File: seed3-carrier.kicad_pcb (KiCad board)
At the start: 2 copper layers, 113 x 61.6 mm, 47 parts, among them J1 AudioJack2, J2 AudioJack2, J3 5V_IN, J4 DISPLAY_UART, J5 SJ1-3535NG, J6 Seed3_PINS_RIGHT, J7 Seed3_PINS_LEFT, U1 TLV9062IDR, U2 TPA6111A2DR

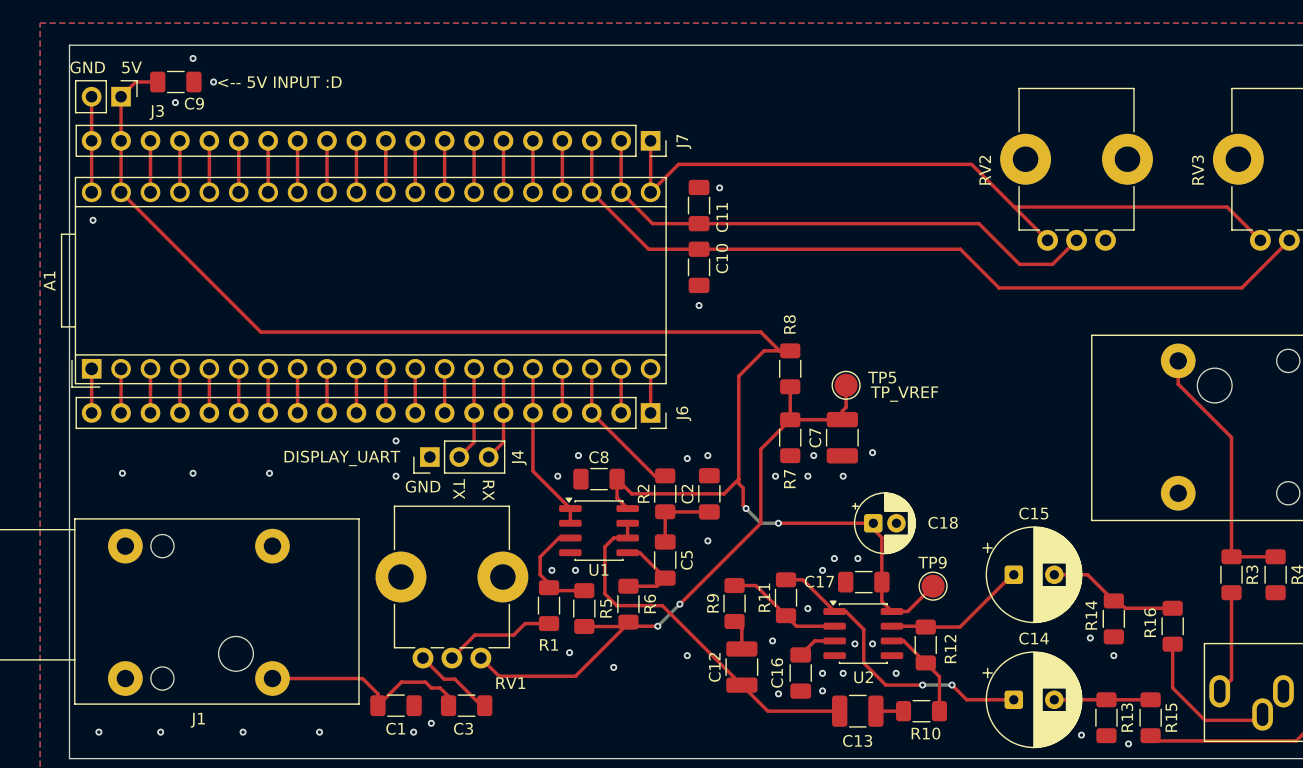
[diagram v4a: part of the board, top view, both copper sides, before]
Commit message: Reposition 5V connector and refine PCB routing
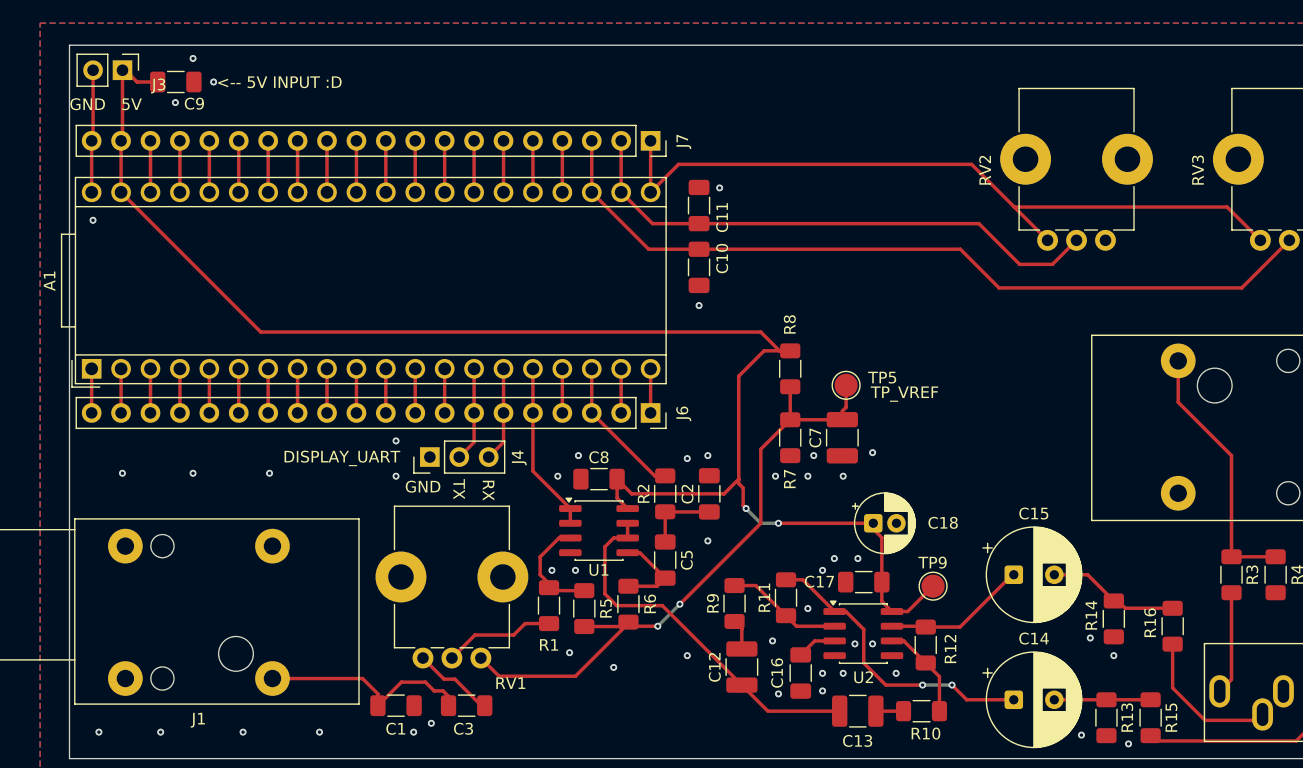
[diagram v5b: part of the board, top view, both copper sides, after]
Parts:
- moved J3 2.29 mm to (55.4, 42.2)
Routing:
- net GND: track 12.1 -> 14.4 mm
- net +5V: track 130.5 -> 132.6 mm
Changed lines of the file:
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@@
 	(footprint "Connector_PinHeader_2.54mm:PinHeader_1x02_P2.54mm_Vertical"
 		(layer "F.Cu")
-		(at 55.25 44.45 -90)
+		(at 55.377 42.164 -90)
 		(descr "Through hole straight pin header, 1x02, 2.54mm pitch, single row")
 		(tags "Through hole pin header THT 1x02 2.54mm single row")
@@
 	)
 	(gr_text "GND"
-		(at 50.8 42.545 0)
+		(at 50.8 45.72 0)
 		(layer "F.SilkS")
 		(effects
@@
 	)
 	(gr_text "5V"
-		(at 55.245 42.545 0)
+		(at 55.245 45.72 0)
 		(layer "F.SilkS")
 		(effects
@@
 	)
 	(segment
-		(start 100.975 67.945)
-		(end 100.975 71.755)
+		(start 52.837 48.138)
+		(end 52.715 48.26)
 		(width 0.3)
 		(layer "F.Cu")
@@
 	)
 	(segment
-		(start 52.715 52.705)
-		(end 52.715 48.26)
+		(start 52.837 42.164)
+		(end 52.837 48.138)
 		(width 0.3)
 		(layer "F.Cu")
@@
 	)
 	(segment
-		(start 52.71 48.255)
+		(start 100.975 67.945)
+		(end 100.975 71.755)
+		(width 0.3)
+		(layer "F.Cu")
+		(net "GND")
+	)
+	(segment
+		(start 52.715 52.705)
 		(end 52.715 48.26)
 		(width 0.3)
@@
 	)
 	(segment
-		(start 52.71 44.45)
-		(end 52.71 48.255)
+		(start 52.71 48.255)
+		(end 52.715 48.26)
 		(width 0.3)
 		(layer "F.Cu")
@@
 	)
 	(segment
-		(start 83.5275 96.2275)
-		(end 82.804 95.504)
+		(start 81.534 94.996)
+		(end 79.4635 94.996)
 		(width 0.3)
 		(layer "F.Cu")
@@
 	)
 	(segment
-		(start 77.4315 96.012)
-		(end 77.4315 97.028)
+		(start 83.5275 96.2275)
+		(end 83.058 95.758)
 		(width 0.3)
 		(layer "F.Cu")
@@
 	)
 	(segment
-		(start 82.804 95.504)
-		(end 82.042 95.504)
+		(start 77.4315 96.012)
+		(end 77.4315 97.028)
 		(width 0.3)
 		(layer "F.Cu")
@@
 	)
 	(segment
-		(start 79.4635 94.996)
-		(end 77.4315 97.028)
+		(start 82.296 95.758)
+		(end 81.534 94.996)
 		(width 0.3)
 		(layer "F.Cu")
@@
 	)
 	(segment
-		(start 83.5275 97.028)
-		(end 83.5275 96.2275)
+		(start 68.326 94.685)
+		(end 76.1045 94.685)
 		(width 0.3)
 		(layer "F.Cu")
@@
 	)
 	(segment
-		(start 82.042 95.504)
-		(end 81.534 94.996)
+		(start 83.058 95.758)
+		(end 82.296 95.758)
 		(width 0.3)
 		(layer "F.Cu")
@@
 	)
 	(segment
-		(start 68.326 94.685)
-		(end 76.1045 94.685)
+		(start 83.5275 97.028)
+		(end 83.5275 96.2275)
 		(width 0.3)
 		(layer "F.Cu")
@@
 	)
 	(segment
-		(start 81.534 94.996)
-		(end 79.4635 94.996)
+		(start 79.4635 94.996)
+		(end 77.4315 97.028)
 		(width 0.3)
 		(layer "F.Cu")
@@
 	(segment
 		(start 151.13 84.175)
-		(end 151.13 73.866054)
+		(end 151.13 75.438)
 		(width 0.3)
 		(layer "F.Cu")
@@
 	)
 	(segment
-		(start 154.94 84.175)
-		(end 151.13 84.175)
+		(start 146.532349 70.840349)
+		(end 146.532349 67.26)
 		(width 0.3)
 		(layer "F.Cu")
@@
 	)
 	(segment
-		(start 146.532349 69.268403)
-		(end 146.532349 67.26)
+		(start 154.94 84.175)
+		(end 151.13 84.175)
 		(width 0.3)
 		(layer "F.Cu")
@@
 	)
 	(segment
-		(start 151.13 73.866054)
-		(end 146.532349 69.268403)
+		(start 151.13 75.438)
+		(end 146.532349 70.840349)
 		(width 0.3)
 		(layer "F.Cu")
@@
 	)
 	(segment
-		(start 86.6525 97.028)
-		(end 86.36 97.028)
+		(start 84.074 94.742)
+		(end 83.144 94.742)
 		(width 0.3)
 		(layer "F.Cu")
@@
 	)
 	(segment
-		(start 84.074 94.742)
-		(end 83.144 94.742)
+		(start 86.6525 97.028)
+		(end 86.36 97.028)
 		(width 0.3)
 		(layer "F.Cu")
@@
 	)
 	(segment
-		(start 55.255 44.455)
-		(end 55.25 44.45)
-		(width 0.3)
-		(layer "F.Cu")
-		(net "+5V")
-	)
-	(segment
-		(start 55.255 48.26)
-		(end 55.255 44.455)
+		(start 55.626 42.164)
+		(end 56.642 43.18)
 		(width 0.3)
 		(layer "F.Cu")
@@
 	)
 	(segment
-		(start 58.42 43.18)
-		(end 56.52 43.18)
+		(start 56.642 43.18)
+		(end 58.42 43.18)
 		(width 0.3)
 		(layer "F.Cu")
@@
 	)
 	(segment
+		(start 55.377 42.164)
+		(end 55.377 48.138)
+		(width 0.3)
+		(layer "F.Cu")
+		(net "+5V")
+	)
+	(segment
 		(start 123.175 88.9)
 		(end 125.365 86.71)
@@
 	)
 	(segment
-		(start 56.52 43.18)
-		(end 55.25 44.45)
+		(start 55.377 48.138)
+		(end 55.255 48.26)
+		(width 0.3)
+		(layer "F.Cu")
+		(net "+5V")
+	)
+	(segment
+		(start 55.377 42.164)
+		(end 55.626 42.164)
 		(width 0.3)
 		(layer "F.Cu")

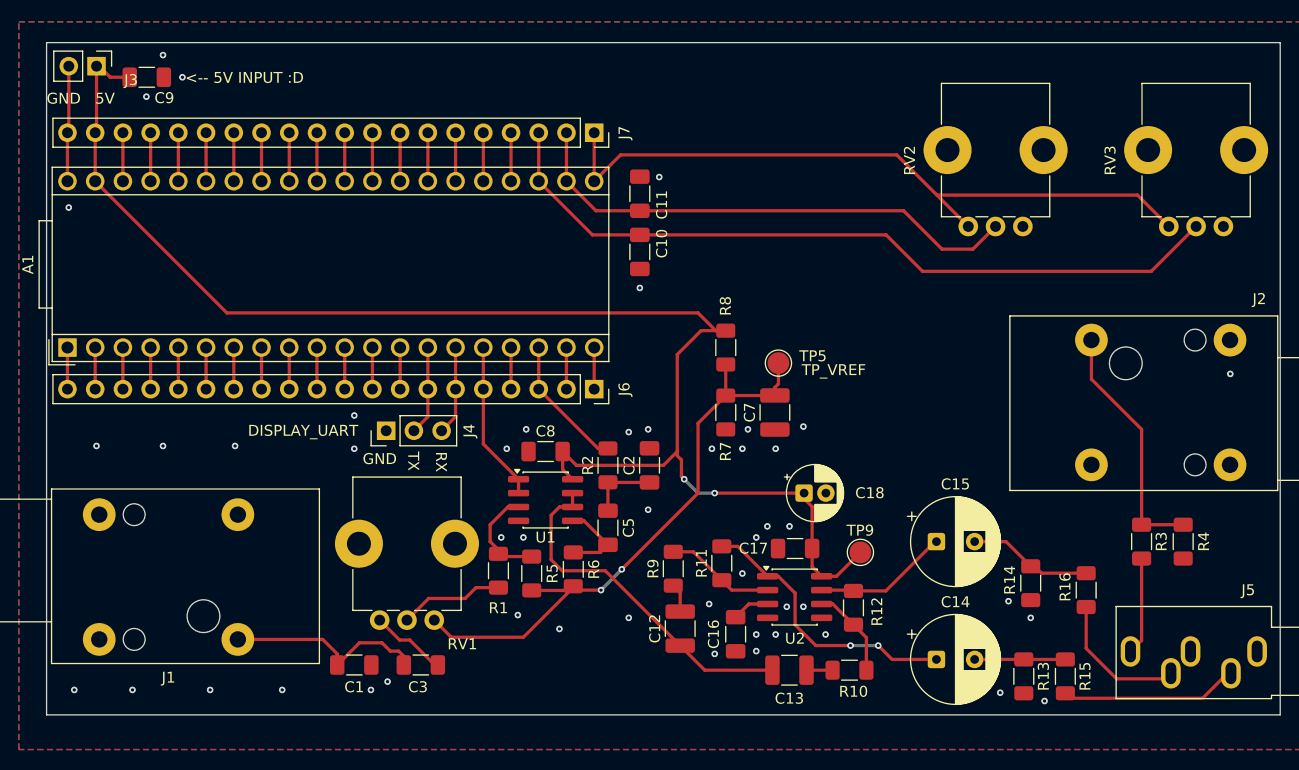
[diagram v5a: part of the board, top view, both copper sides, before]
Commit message: Remove ground stitching vias
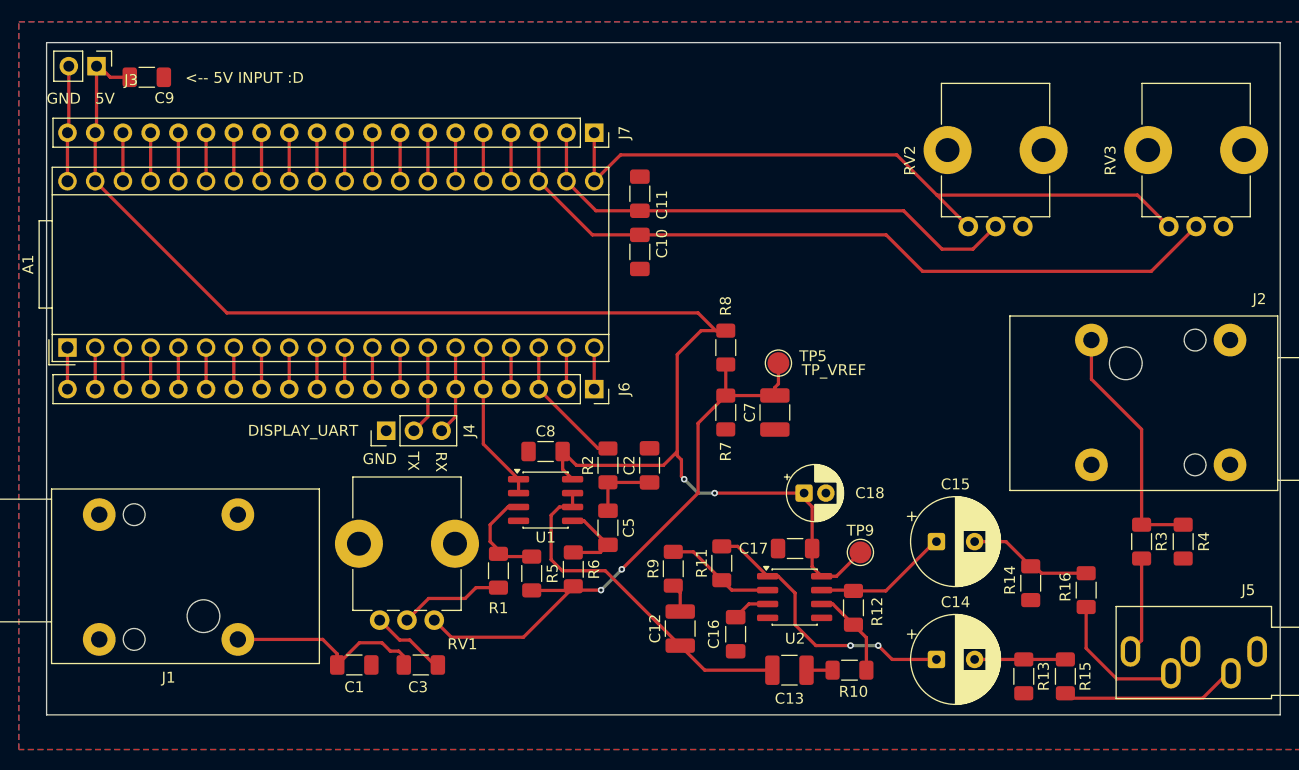
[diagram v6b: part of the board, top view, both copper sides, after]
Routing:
- net GND: vias 49 -> 0

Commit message: Add volume and tone knob silkscreen labels
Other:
- board text added: "TONE"
- board text added: "VOLUME"
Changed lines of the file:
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@@
+		)
+	)
+	(gr_text "VOLUME"
+		(at 134.874 59.944 0)
+		(layer "F.SilkS")
+		(effects
+			(font
+				(size 1 1)
+				(thickness 0.1)
+			)
+			(justify left bottom)
+		)
+	)
+	(gr_text "TONE"
+		(at 154.178 59.944 0)
+		(layer "F.SilkS")
+		(effects
+			(font
+				(size 1 1)
+				(thickness 0.1)
+			)
+			(justify left bottom)
 		)
 	)

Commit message: Add local ground stitching vias and adjust silkscreen labels
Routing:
- net GND: vias 0 -> 16
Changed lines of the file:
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@@
 		(tags "resistor handsolder")
 		(property "Reference" "R1"
-			(at -3.429 0 0)
+			(at -3.429 0 90)
 			(layer "F.SilkS")
 			(effects
@@
 		(tags "resistor handsolder")
 		(property "Reference" "R5"
-			(at 0 1.905 90)
+			(at -3.556 0 270)
 			(layer "F.SilkS")
 			(effects
@@
 		(tags "capacitor handsolder")
 		(property "Reference" "C2"
-			(at 0 -1.85 90)
+			(at 0.762 1.905 90)
 			(layer "F.SilkS")
 			(effects
@@
 		(tags "capacitor handsolder")
 		(property "Reference" "C16"
-			(at 0 2 90)
+			(at -0.484 2 90)
 			(layer "F.SilkS")
 			(effects
@@
 		(tags "capacitor handsolder")
 		(property "Reference" "C10"
-			(at -0.762 -2.032 270)
+			(at 0 -2.794 270)
 			(layer "F.SilkS")
 			(effects
@@
 		(tags "resistor handsolder")
 		(property "Reference" "R2"
-			(at 0 -1.83 90)
+			(at 0.762 1.905 90)
 			(layer "F.SilkS")
 			(effects
@@
 		(tags "resistor handsolder")
 		(property "Reference" "R8"
-			(at -3.81 0 90)
+			(at 0.127 2.032 90)
 			(layer "F.SilkS")
 			(effects
@@
 		(tags "resistor handsolder")
 		(property "Reference" "R6"
-			(at 0 1.905 90)
+			(at -3.683 0 90)
 			(layer "F.SilkS")
 			(effects
@@
 		(tags "capacitor handsolder")
 		(property "Reference" "C11"
-			(at -1.016 2.032 90)
+			(at 0 2.794 90)
 			(layer "F.SilkS")
 			(effects
@@
 		(tags "resistor handsolder")
 		(property "Reference" "R7"
-			(at 3.575 0 90)
+			(at -0.235 2.032 90)
 			(layer "F.SilkS")
 			(effects
@@
 			(at 0 2.05 0)
 			(layer "F.Fab")
+			(hide yes)
 			(effects
 				(font
@@
 		(tags "capacitor handsolder")
 		(property "Reference" "C7"
-			(at 0 -2.3 90)
+			(at 0.235 2.612 90)
 			(layer "F.SilkS")
 			(effects
@@
 		(net "GND")
 	)
+	(via
+		(at 140.97 92.71)
+		(size 0.6)
+		(drill 0.3)
+		(layers "F.Cu" "B.Cu")
+		(free yes)
+		(net "GND")
+	)
+	(via
+		(at 106.934 52.324)
+		(size 0.6)
+		(drill 0.3)
+		(layers "F.Cu" "B.Cu")
+		(free yes)
+		(net "GND")
+	)
+	(via
+		(at 93.472 77.47)
+		(size 0.6)
+		(drill 0.3)
+		(layers "F.Cu" "B.Cu")
+		(free yes)
+		(net "GND")
+	)
+	(via
+		(at 117.856 84.582)
+		(size 0.6)
+		(drill 0.3)
+		(layers "F.Cu" "B.Cu")
+		(free yes)
+		(net "GND")
+	)
+	(via
+		(at 80.518 98.806)
+		(size 0.6)
+		(drill 0.3)
+		(layers "F.Cu" "B.Cu")
+		(free yes)
+		(net "GND")
+	)
+	(via
+		(at 93.98 85.09)
+		(size 0.6)
+		(drill 0.3)
+		(layers "F.Cu" "B.Cu")
+		(free yes)
+		(net "GND")
+	)
+	(via
+		(at 119.888 75.438)
+		(size 0.6)
+		(drill 0.3)
+		(layers "F.Cu" "B.Cu")
+		(free yes)
+		(net "GND")
+	)
+	(via
+		(at 62.992 43.18)
+		(size 0.6)
+		(drill 0.3)
+		(layers "F.Cu" "B.Cu")
+		(free yes)
+		(net "GND")
+	)
+	(via
+		(at 154.94 88.9)
+		(size 0.6)
+		(drill 0.3)
+		(layers "F.Cu" "B.Cu")
+		(free yes)
+		(net "GND")
+	)
+	(via
+		(at 105.918 75.438)
+		(size 0.6)
+		(drill 0.3)
+		(layers "F.Cu" "B.Cu")
+		(free yes)
+		(net "GND")
+	)
+	(via
+		(at 141.478 58.674)
+		(size 0.6)
+		(drill 0.3)
+		(layers "F.Cu" "B.Cu")
+		(free yes)
+		(net "GND")
+	)
+	(via
+		(at 159.766 58.674)
+		(size 0.6)
+		(drill 0.3)
+		(layers "F.Cu" "B.Cu")
+		(free yes)
+		(net "GND")
+	)
+	(via
+		(at 116.84 93.98)
+		(size 0.6)
+		(drill 0.3)
+		(layers "F.Cu" "B.Cu")
+		(free yes)
+		(net "GND")
+	)
+	(via
+		(at 138.43 99.568)
+		(size 0.6)
+		(drill 0.3)
+		(layers "F.Cu" "B.Cu")
+		(free yes)
+		(net "GND")
+	)
+	(via
+		(at 112.014 95.758)
+		(size 0.6)
+		(drill 0.3)
+		(layers "F.Cu" "B.Cu")
+		(free yes)
+		(net "GND")
+	)
+	(via
+		(at 106.934 60.706)
+		(size 0.6)
+		(drill 0.3)
+		(layers "F.Cu" "B.Cu")
+		(free yes)
+		(net "GND")
+	)
